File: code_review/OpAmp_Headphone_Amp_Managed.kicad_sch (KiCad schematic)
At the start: 18 parts, among them J1 Audio In, J2 Headphone Out, U1 NE5532

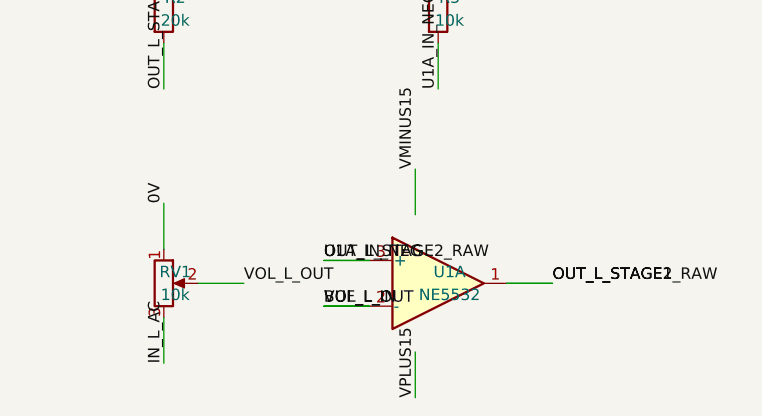
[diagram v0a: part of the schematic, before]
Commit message: fix: flatten extends chain in lib_symbols to fix KiCad 9 load error
- Add read_lib_symbol_def_flat() to sch_doc.py: merges parent geometry
  sub-symbols into child symbol node, removes (extends ...) attribute,
  returns a single self-contained symbol definition
- Add _collect_subsymbols() and _rename_subsymbol() helpers
- Update _embed_symbol_if_found() in netlist.py to use flat function
  instead of chain embedding (which caused LM2904 parent reference)
- Regenerate OpAmp_Headphone_Amp schematic: 0 LM2904/extends refs
- Verified KiCad 9.0.7 loads both schematics cleanly (exit 0)
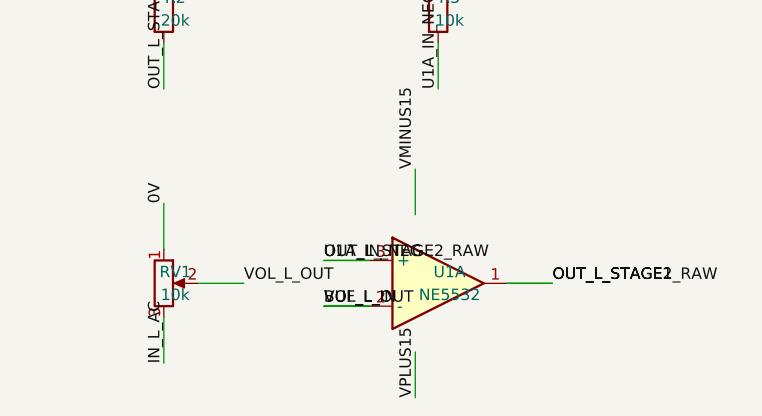
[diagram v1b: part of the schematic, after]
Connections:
- net BUF_L_IN: now also U1.2 (-)
- net OUT_L_STAGE1: now also U1.1, U1.3 (+)
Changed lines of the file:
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@@
         "OpAmp_Headphone_Amp"
         (path
-          "/e19b14c0-045c-4013-aa58-74bf58c9f4d4/"
+          "/40a7504e-231a-4d42-8382-f13134e62349/"
           (reference "C1")
           (unit 1)
@@
         "OpAmp_Headphone_Amp"
         (path
-          "/e19b14c0-045c-4013-aa58-74bf58c9f4d4/"
+          "/40a7504e-231a-4d42-8382-f13134e62349/"
           (reference "C2")
           (unit 1)
@@
         "OpAmp_Headphone_Amp"
         (path
-          "/e19b14c0-045c-4013-aa58-74bf58c9f4d4/"
+          "/40a7504e-231a-4d42-8382-f13134e62349/"
           (reference "C3")
           (unit 1)
@@
         "OpAmp_Headphone_Amp"
         (path
-          "/e19b14c0-045c-4013-aa58-74bf58c9f4d4/"
+          "/40a7504e-231a-4d42-8382-f13134e62349/"
           (reference "C4")
           (unit 1)
@@
         "OpAmp_Headphone_Amp"
         (path
-          "/e19b14c0-045c-4013-aa58-74bf58c9f4d4/"
+          "/40a7504e-231a-4d42-8382-f13134e62349/"
           (reference "C5")
           (unit 1)
@@
         "OpAmp_Headphone_Amp"
         (path
-          "/e19b14c0-045c-4013-aa58-74bf58c9f4d4/"
+          "/40a7504e-231a-4d42-8382-f13134e62349/"
           (reference "C6")
           (unit 1)
@@
         "OpAmp_Headphone_Amp"
         (path
-          "/e19b14c0-045c-4013-aa58-74bf58c9f4d4/"
+          "/40a7504e-231a-4d42-8382-f13134e62349/"
           (reference "C7")
           (unit 1)
@@
         "OpAmp_Headphone_Amp"
         (path
-          "/e19b14c0-045c-4013-aa58-74bf58c9f4d4/"
+          "/40a7504e-231a-4d42-8382-f13134e62349/"
           (reference "J1")
           (unit 1)
@@
         "OpAmp_Headphone_Amp"
         (path
-          "/e19b14c0-045c-4013-aa58-74bf58c9f4d4/"
+          "/40a7504e-231a-4d42-8382-f13134e62349/"
           (reference "J2")
           (unit 1)
@@
         "OpAmp_Headphone_Amp"
         (path
-          "/e19b14c0-045c-4013-aa58-74bf58c9f4d4/"
+          "/40a7504e-231a-4d42-8382-f13134e62349/"
           (reference "R1")
           (unit 1)
@@
         "OpAmp_Headphone_Amp"
         (path
-          "/e19b14c0-045c-4013-aa58-74bf58c9f4d4/"
+          "/40a7504e-231a-4d42-8382-f13134e62349/"
           (reference "R2")
           (unit 1)
@@
         "OpAmp_Headphone_Amp"
         (path
-          "/e19b14c0-045c-4013-aa58-74bf58c9f4d4/"
+          "/40a7504e-231a-4d42-8382-f13134e62349/"
           (reference "R3")
           (unit 1)
@@
         "OpAmp_Headphone_Amp"
         (path
-          "/e19b14c0-045c-4013-aa58-74bf58c9f4d4/"
+          "/40a7504e-231a-4d42-8382-f13134e62349/"
           (reference "R4")
           (unit 1)
@@
         "OpAmp_Headphone_Amp"
         (path
-          "/e19b14c0-045c-4013-aa58-74bf58c9f4d4/"
+          "/40a7504e-231a-4d42-8382-f13134e62349/"
           (reference "R5")
           (unit 1)
@@
         "OpAmp_Headphone_Amp"
         (path
-          "/e19b14c0-045c-4013-aa58-74bf58c9f4d4/"
+          "/40a7504e-231a-4d42-8382-f13134e62349/"
           (reference "R6")
           (unit 1)
@@
         "OpAmp_Headphone_Amp"
         (path
-          "/e19b14c0-045c-4013-aa58-74bf58c9f4d4/"
+          "/40a7504e-231a-4d42-8382-f13134e62349/"
           (reference "R7")
           (unit 1)
@@
         "OpAmp_Headphone_Amp"
         (path
-          "/e19b14c0-045c-4013-aa58-74bf58c9f4d4/"
+          "/40a7504e-231a-4d42-8382-f13134e62349/"
           (reference "RV1")
           (unit 1)
@@
         "OpAmp_Headphone_Amp"
         (path
-          "/e19b14c0-045c-4013-aa58-74bf58c9f4d4/"
+          "/40a7504e-231a-4d42-8382-f13134e62349/"
           (reference "U1")
           (unit 1)
@@
     (effects (font (size 1.27 1.27)) (justify left) hide)
   )
-  (sheet_instances (path "/e19b14c0-045c-4013-aa58-74bf58c9f4d4/" (page "1")))
+  (sheet_instances (path "/40a7504e-231a-4d42-8382-f13134e62349/" (page "1")))
 )
